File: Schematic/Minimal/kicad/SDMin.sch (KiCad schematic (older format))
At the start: 86 parts

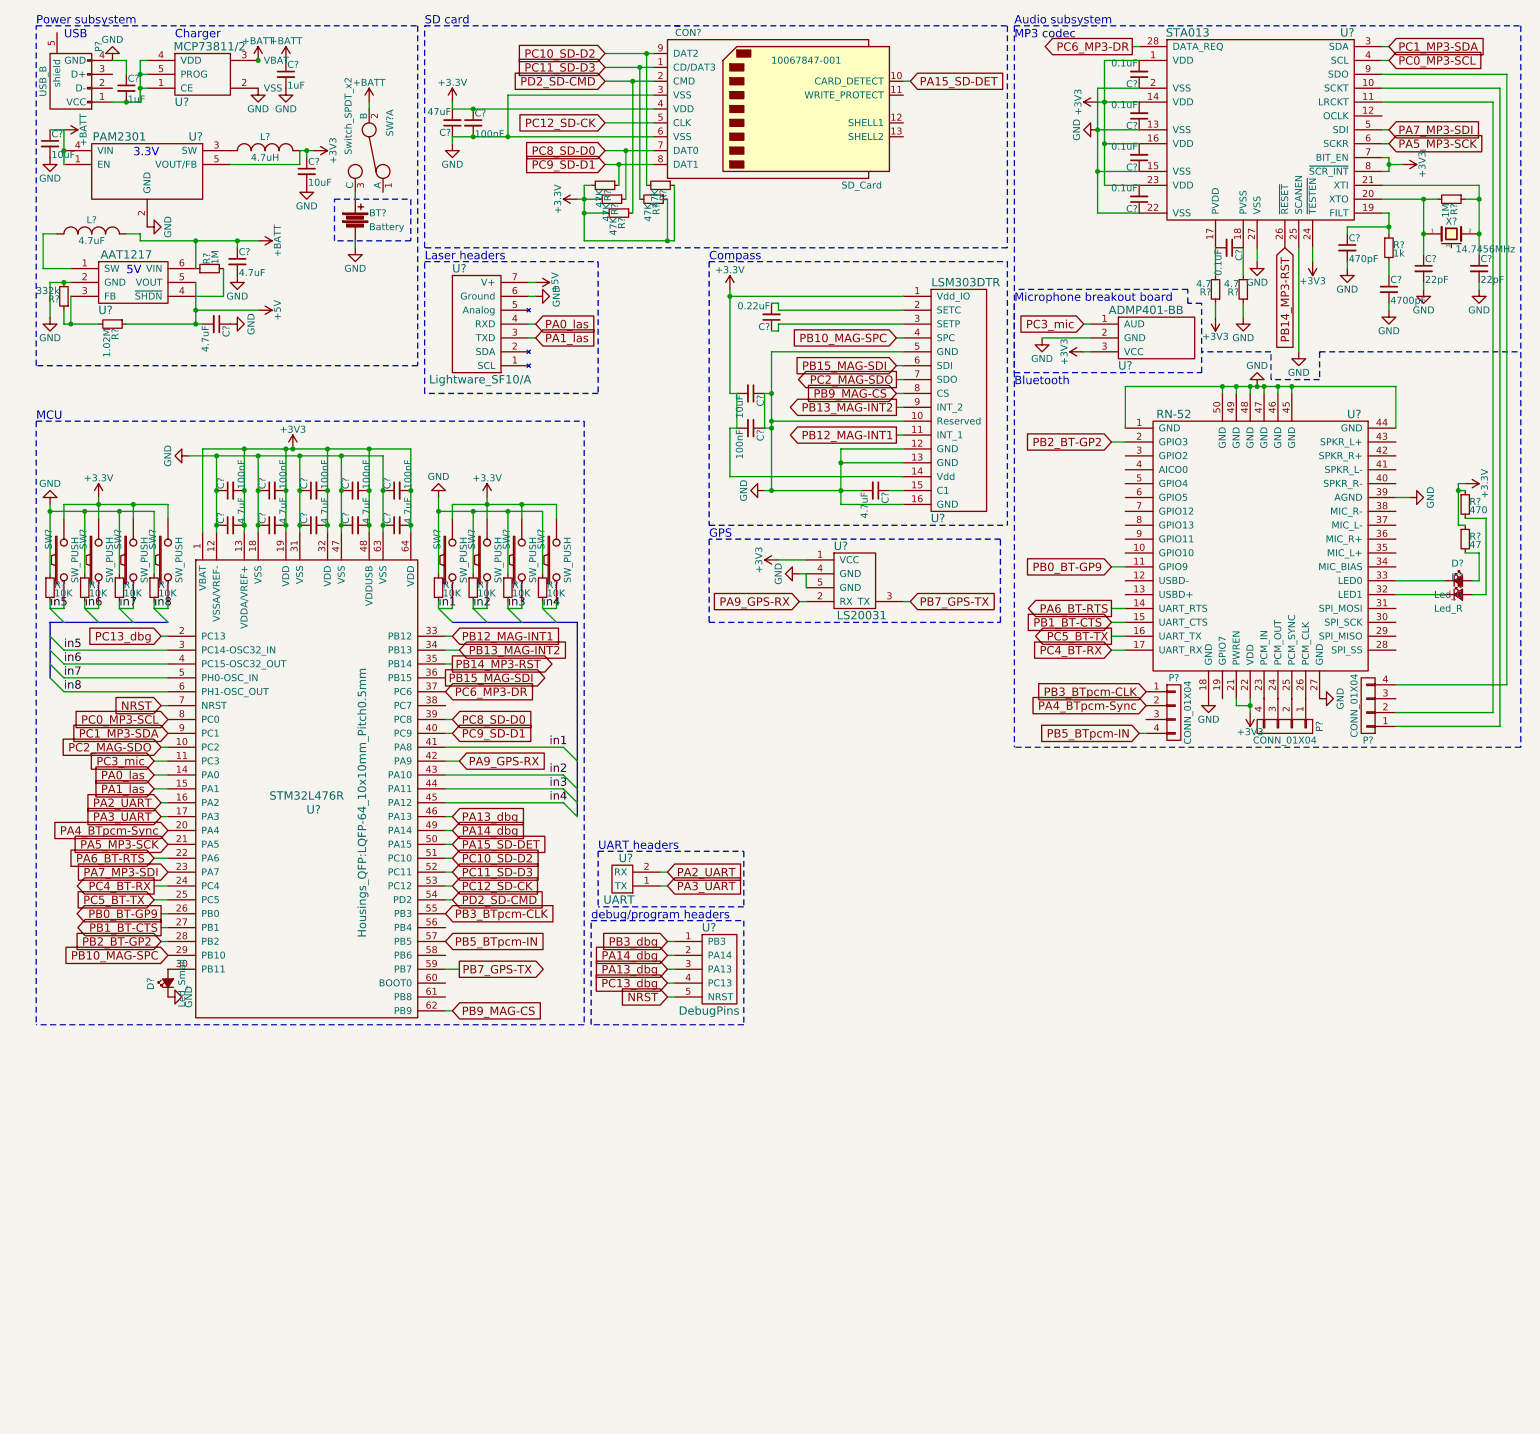
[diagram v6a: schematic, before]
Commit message: Assign some footprints to schematic
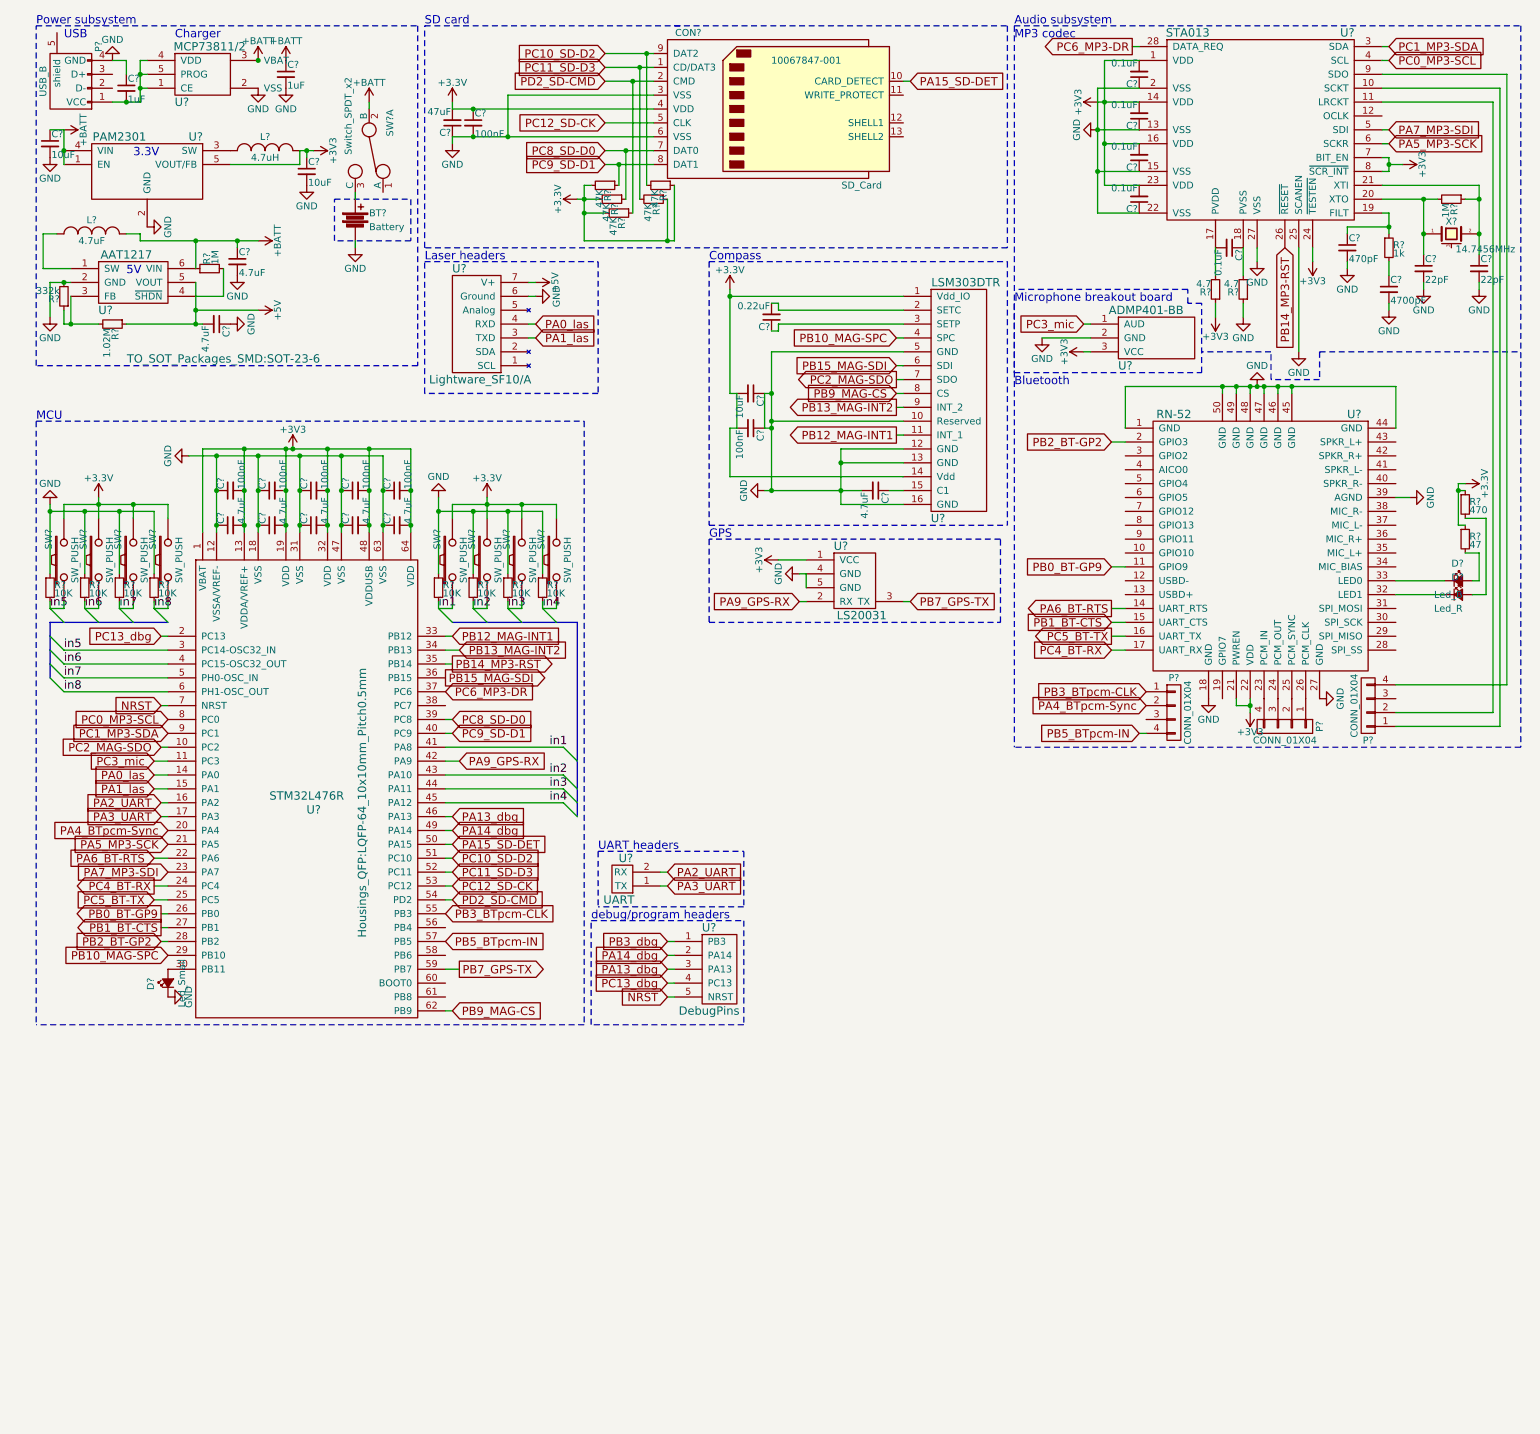
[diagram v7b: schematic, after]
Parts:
- P?: footprint (none) -> Connect:USB_Micro-B
- SW?: footprint (none) -> Buttons_Switches_ThroughHole:SW_Micro_SPST
- U?: footprint (none) -> con-trougnouf:Socket_Strip_Straight_1x04_3467
- U? (x2): footprint (none) -> TO_SOT_Packages_SMD:SOT-23-5
- U?: footprint (none) -> TO_SOT_Packages_SMD:SOT-23-6

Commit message: Update schematic, change compass (LGA->QFN)
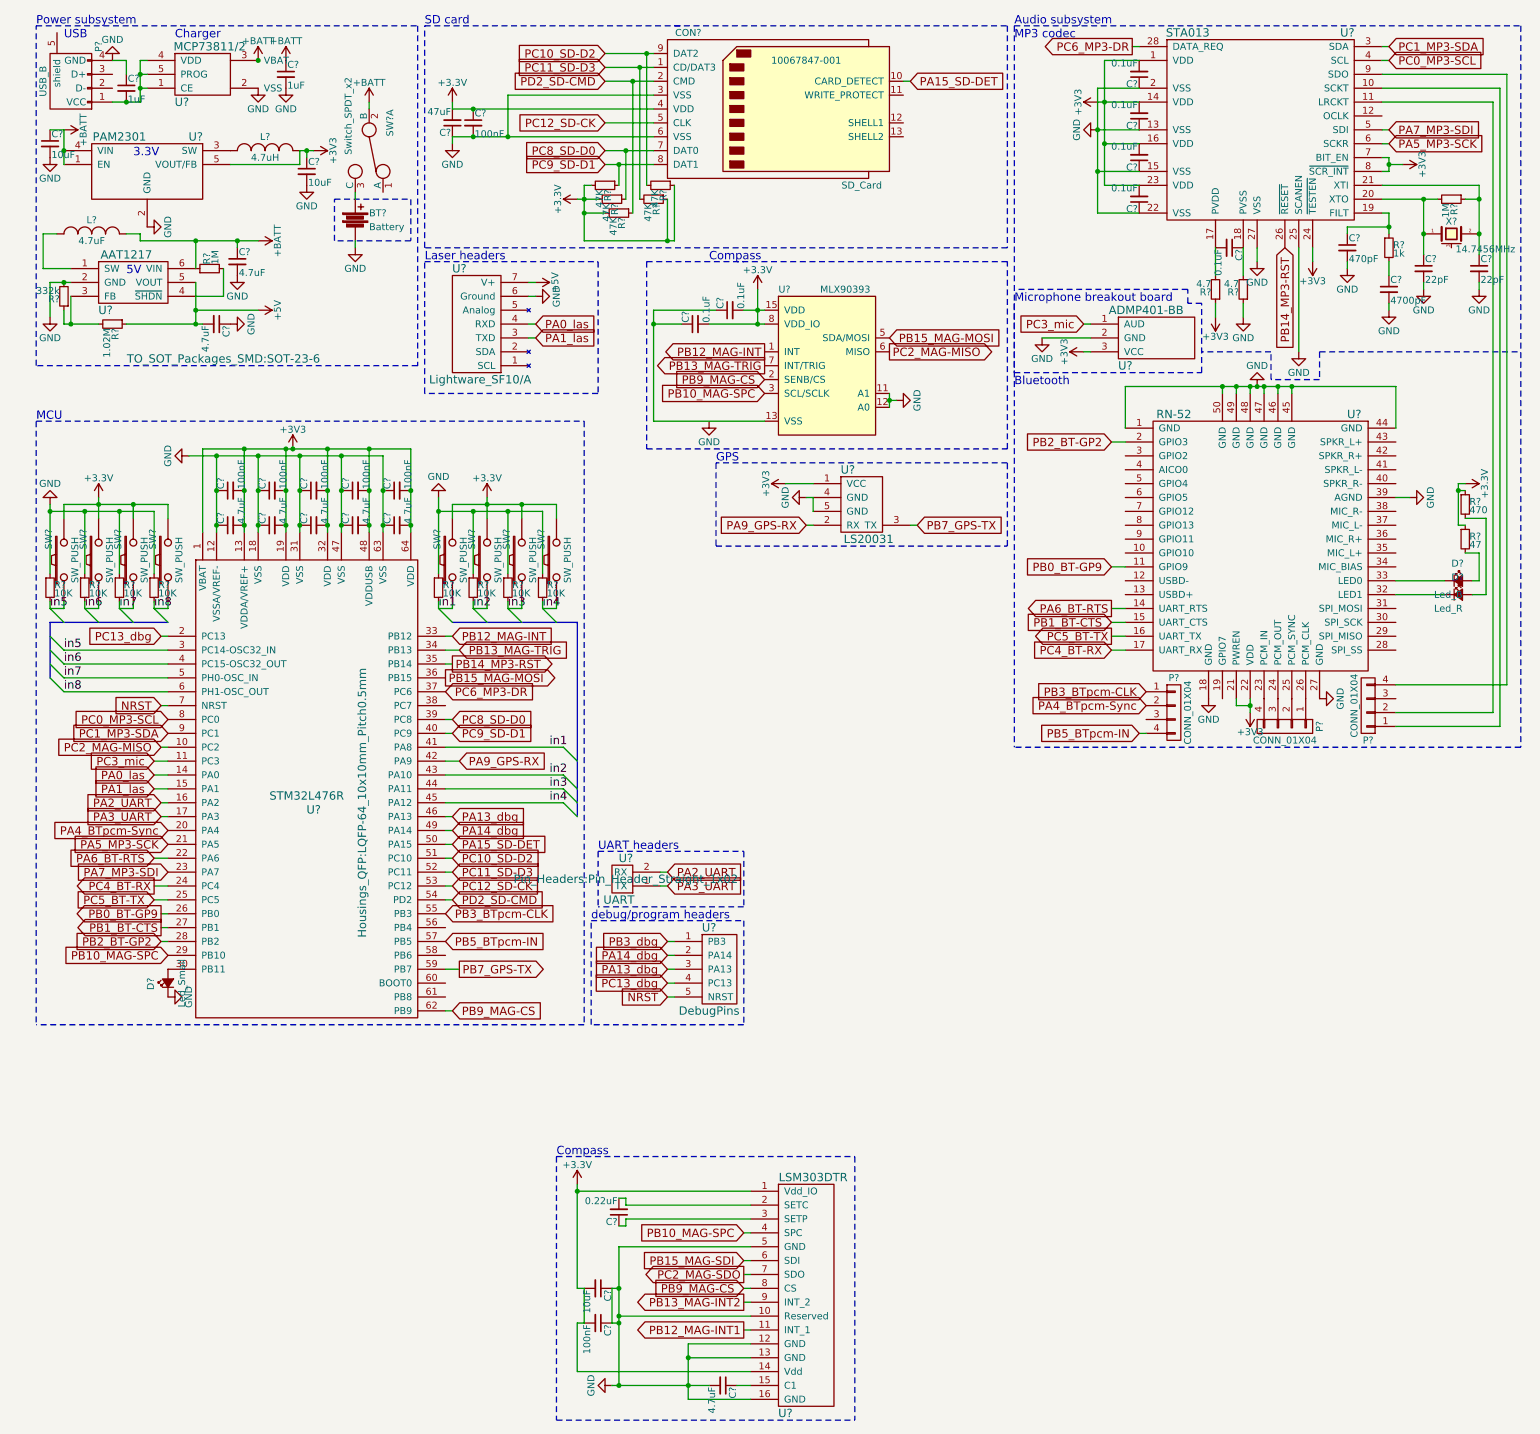
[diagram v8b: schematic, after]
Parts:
- removed C?: 4.7uF, symbol C_Small
- removed C?: 0.22uF, symbol C_Small
- removed C?: 10uF, symbol C_Small
- removed C?: 100nF, symbol C_Small
- removed U?: LSM303DTR, symbol LSM303DTR
- added C?: 4.7uF, symbol C_Small
- added C?: 0.22uF, symbol C_Small
- added C?: 10uF, symbol C_Small
- added C?: 100nF, symbol C_Small
- added C? (x2): 0.1uF, symbol C_Small
- added U?: LSM303DTR, symbol LSM303DTR
- added U?: MLX90393, symbol MLX90393
- U?: footprint (none) -> Pin_Headers:Pin_Header_Straight_1x02
- U?: footprint (none) -> Pin_Headers:Pin_Header_Straight_1x05
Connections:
- net +3V3: now also C?.2, C?.2, C?.2, C?.2, U?.1 (Vdd_IO), U?.14 (Vdd), U?.15 (VDD), U?.8 (VDD_IO)
- net GND: now also C?.1, C?.1, C?.2, U?.10 (Reserved), U?.11 (A1), U?.12 (A0), U?.12 (GND), U?.13 (GND), U?.16 (GND), U?.5 (GND)
- net PB10_MAG-SPC: now also U?.3 (SCL/SCLK), U?.4 (SPC)
- net PB12_MAG-INT1: now also U?.11 (INT_1); no longer U?.33 (PB12)
- net PB13_MAG-INT2: now also U?.9 (INT_2); no longer U?.34 (PB13)
- net PB15_MAG-SDI: now also U?.6 (SDI); no longer U?.36 (PB15)
- net PB9_MAG-CS: now also U?.2 (SENB/CS), U?.8 (CS)
- net PC2_MAG-SDO: now also U?.7 (SDO); no longer U?.10 (PC2)
- new net: C?.1, U?.15 (C1)
- new net: C?.2, U?.2 (SETC)
- new net: C?.1, U?.3 (SETP)
- new net: C?.1, C?.1, U?.13 (VSS)
- new net PB12_MAG-INT: U?.1 (INT), U?.33 (PB12)
- new net PB13_MAG-TRIG: U?.34 (PB13), U?.7 (INT/TRIG)
- new net PB15_MAG-MOSI: U?.36 (PB15), U?.5 (SDA/MOSI)
- new net PC2_MAG-MISO: U?.10 (PC2), U?.6 (MISO)
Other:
- moved on the sheet: U?
